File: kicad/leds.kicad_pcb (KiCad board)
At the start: 2 copper layers, 45.3 x 51.3 mm, 15 parts, among them P1 WJ127-5.0-2P, Q1 IRF7201, Q2 IRF7201, Q3 IRF7201, U1 ESP-F, U3 LM2575HVS-3.3_C347428

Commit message: changed the pcb file to add headers
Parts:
- added J1: Conn_01x04, Connector_PinHeader_2.54mm:PinHeader_1x04_P2.54mm_Vertical, F.Cu at (52.1, 63.5)
- C1, C2: footprint Capacitor_THT:CP_Radial_D8.0mm_P3.50mm -> easyeda2kicad:CAP-SMD_BD6.3-L6.6-W6.6-FD
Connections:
- net Net-(U1-EN) renamed VCC
- U1 pad 21: unconnected-(U1-RXD-Pad21) -> Net-(J1-Pin_4)
- U1 pad 22: unconnected-(U1-TXD-Pad22) -> Net-(J1-Pin_3)
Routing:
- net Net-(J1-Pin_4): track 0.00 -> 67.2 mm, vias 0 -> 2
- net Net-(J1-Pin_3): track 0.00 -> 63.8 mm, vias 0 -> 1
- net VCC: track 94.8 -> 109.7 mm
- net Net-(P1-+): track 58.3 -> 54.0 mm

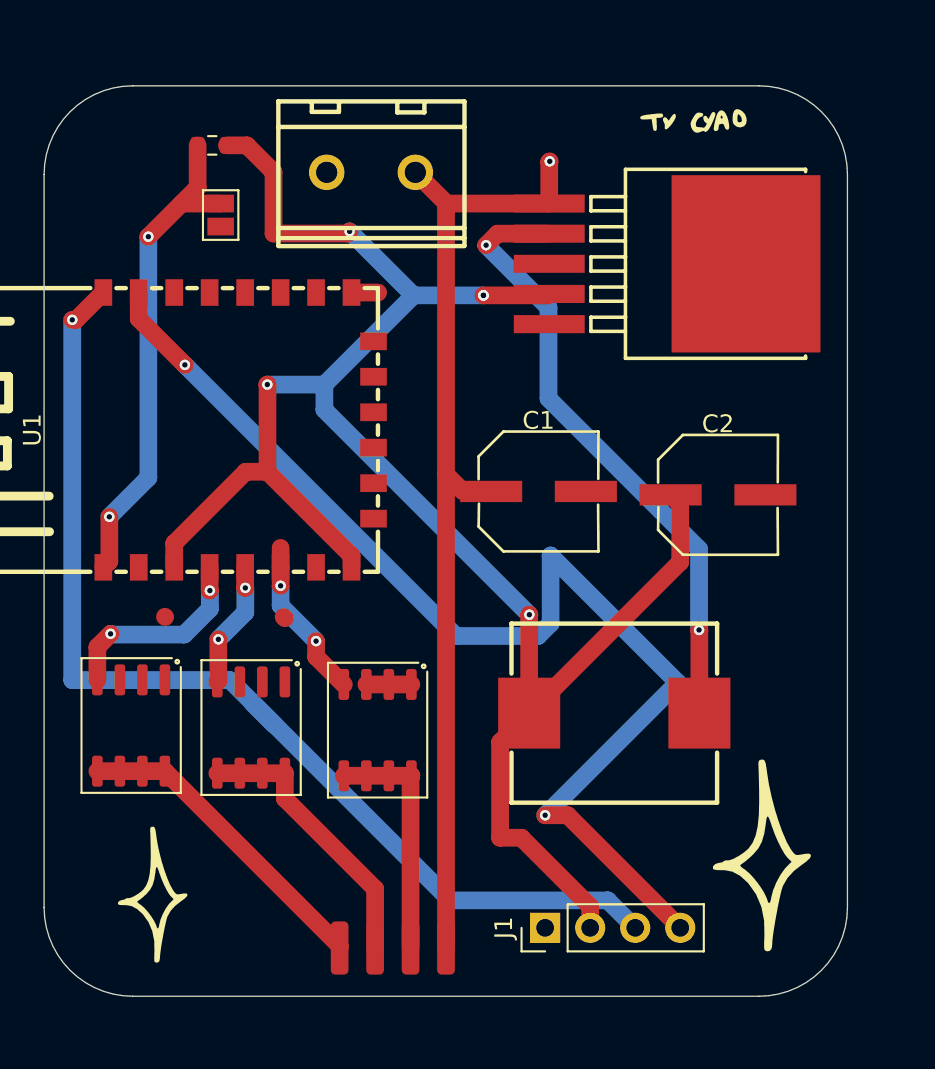
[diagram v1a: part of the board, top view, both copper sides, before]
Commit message: changed the silkscreen :3c
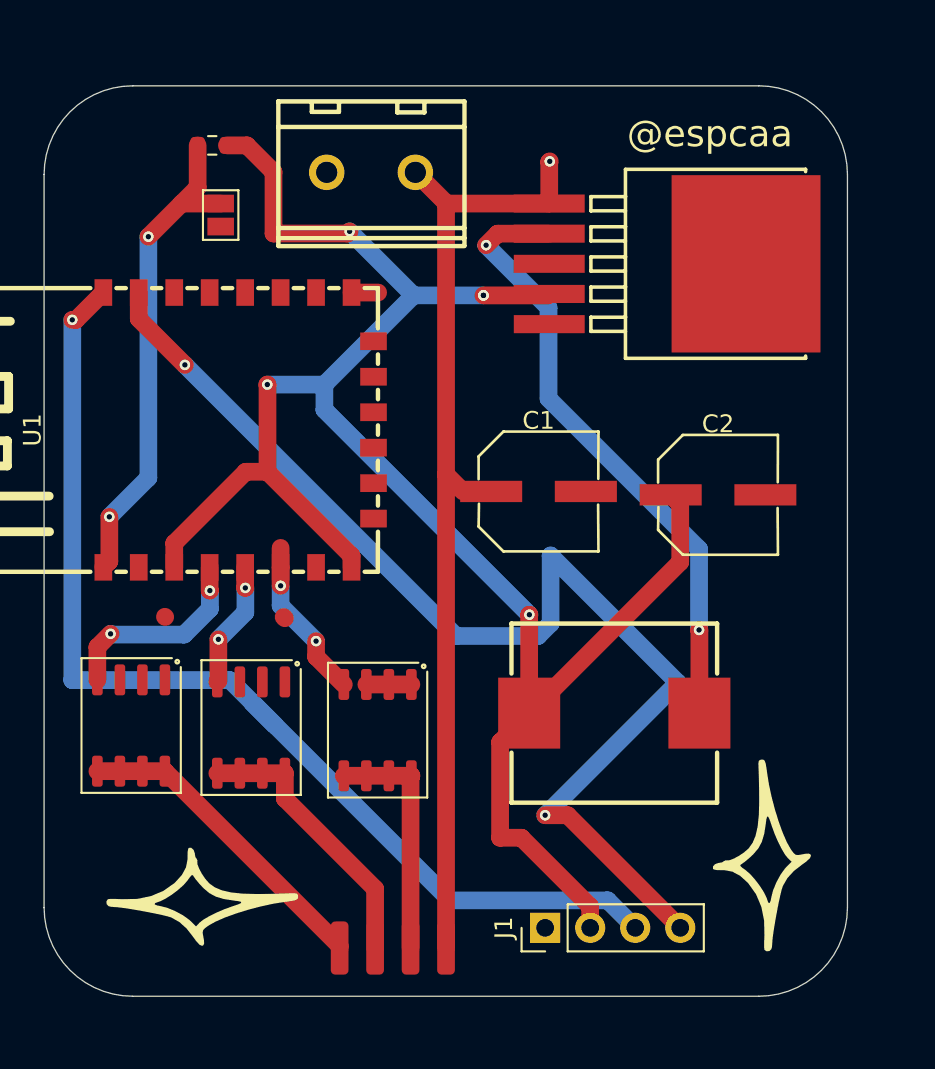
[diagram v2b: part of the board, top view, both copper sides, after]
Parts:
- removed the G*** at (61.0, 20.3)
- removed the G*** at (30.3, 63.3)
- added G***: LOGO, LOGO, F.Cu at (30.4, 62.2)
- added G***: LOGO, LOGO, B.Cu at (60.5, 43.9)
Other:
- board text added: "@espcaa"
